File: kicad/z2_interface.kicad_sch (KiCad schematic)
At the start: 0 parts

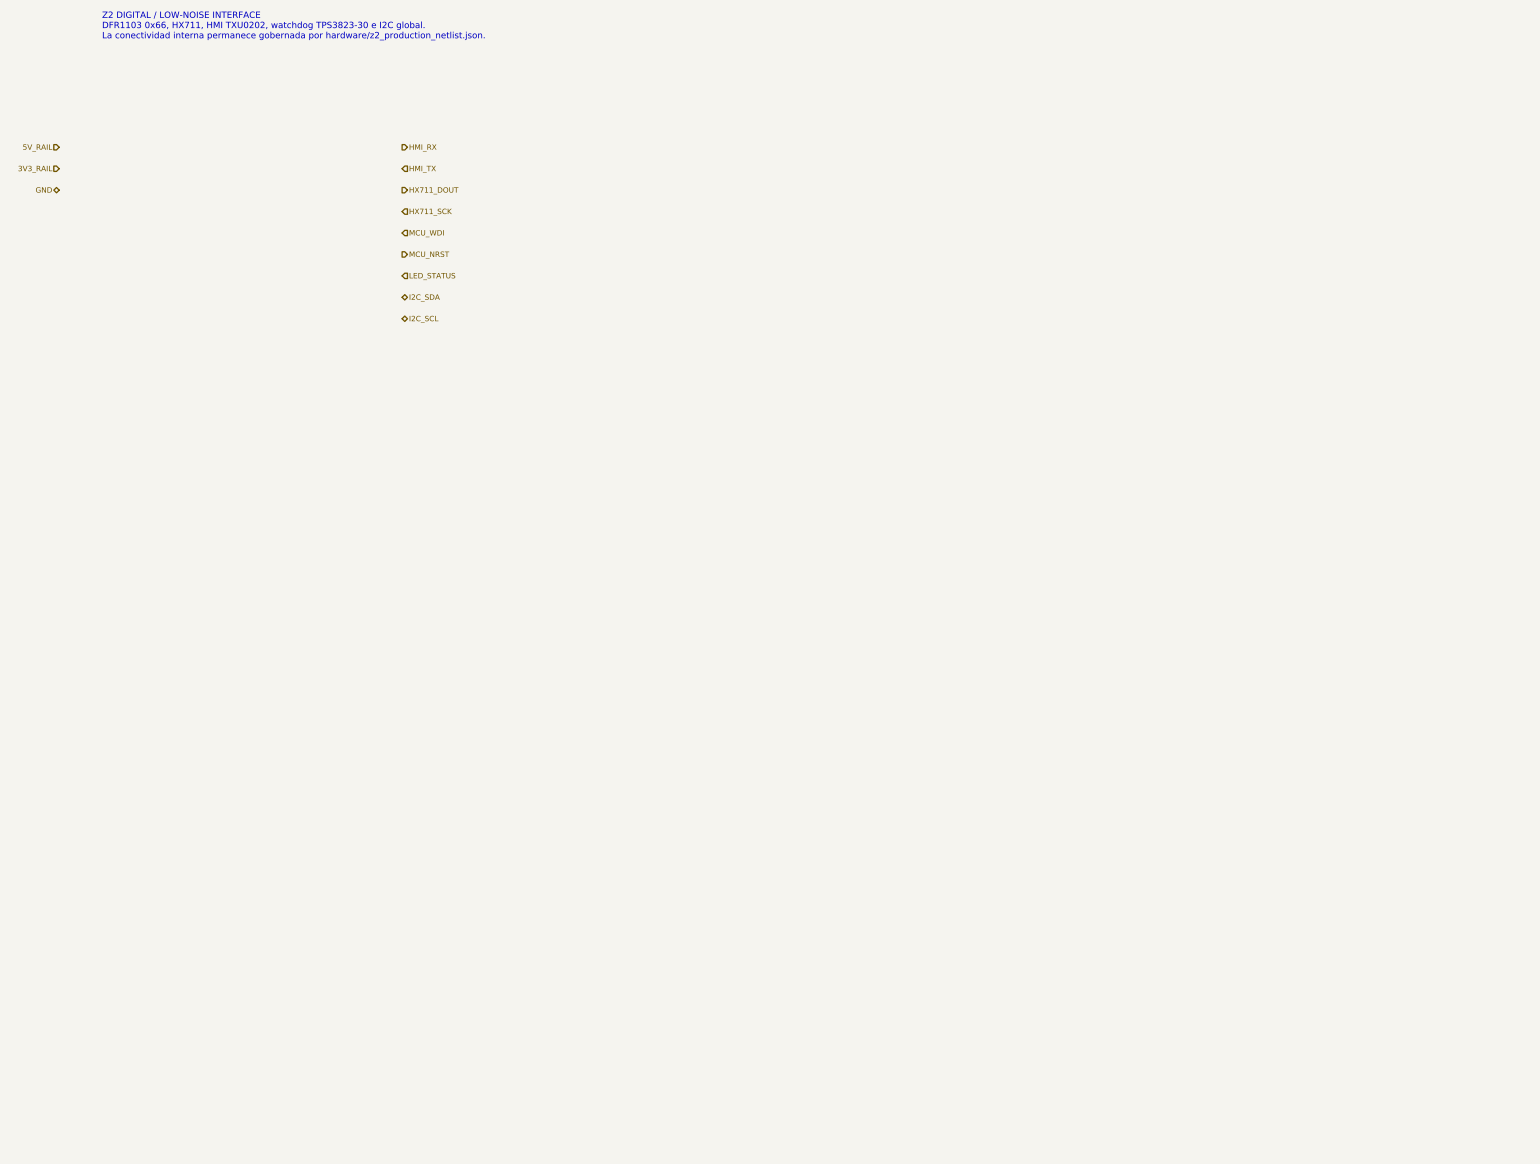
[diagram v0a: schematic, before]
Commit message: eda: materializar hierarchy de producción y cerrar ERC en cero (#15)
Materializa Z0–Z4 de forma determinista desde JSON/BOM, registra NFB_GEN, cierra seis links físicos verificados, elimina la deuda ERC de PR #14 y congela ERC=0/0 antes de placement. Mantiene placement, routing y geometría PCB fuera de alcance.
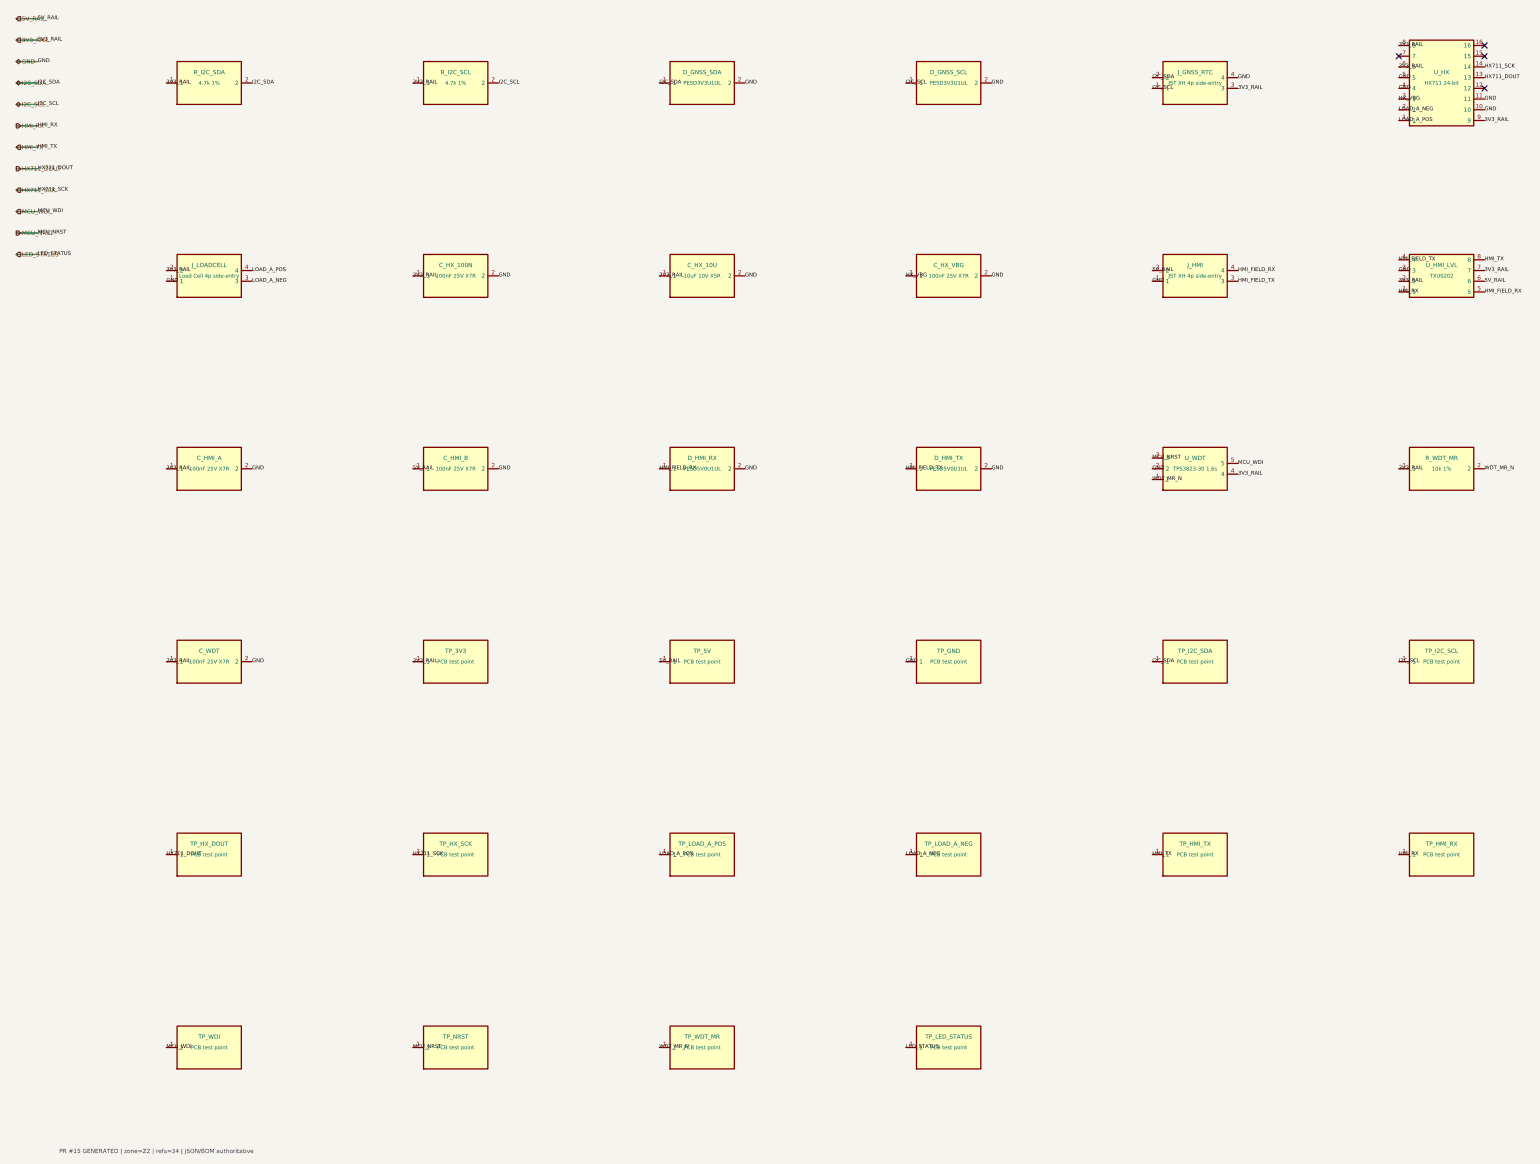
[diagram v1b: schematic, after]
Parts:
- added C_HMI_A: 100nF 25V X7R, Capacitor_SMD:C_0402_1005Metric, symbol NFB_GEN:SYM_C_HMI_A
- added C_HMI_B: 100nF 25V X7R, Capacitor_SMD:C_0402_1005Metric, symbol NFB_GEN:SYM_C_HMI_B
- added C_HX_100N: 100nF 25V X7R, Capacitor_SMD:C_0402_1005Metric, symbol NFB_GEN:SYM_C_HX_100N
- added C_HX_10U: 10uF 10V X5R, Capacitor_SMD:C_0805_2012Metric, symbol NFB_GEN:SYM_C_HX_10U
- added C_HX_VBG: 100nF 25V X7R, Capacitor_SMD:C_0402_1005Metric, symbol NFB_GEN:SYM_C_HX_VBG
- added C_WDT: 100nF 25V X7R, Capacitor_SMD:C_0402_1005Metric, symbol NFB_GEN:SYM_C_WDT
- added D_GNSS_SCL: PESD3V3U1UL, Diode_SMD:D_SOD-882, symbol NFB_GEN:SYM_D_GNSS_SCL
- added D_GNSS_SDA: PESD3V3U1UL, Diode_SMD:D_SOD-882, symbol NFB_GEN:SYM_D_GNSS_SDA
- added D_HMI_RX: PESD5V0U1UL, Diode_SMD:D_SOD-882, symbol NFB_GEN:SYM_D_HMI_RX
- added D_HMI_TX: PESD5V0U1UL, Diode_SMD:D_SOD-882, symbol NFB_GEN:SYM_D_HMI_TX
- added J_GNSS_RTC: JST XH 4p side-entry, Connector_JST:JST_XH_S4B-XH-A_1x04_P2.50mm_Horizontal, symbol NFB_GEN:SYM_J_GNSS_RTC
- added J_HMI: JST XH 4p side-entry, Connector_JST:JST_XH_S4B-XH-A_1x04_P2.50mm_Horizontal, symbol NFB_GEN:SYM_J_HMI
- added J_LOADCELL: Load Cell 4p side-entry, TerminalBlock_Phoenix:TerminalBlock_Phoenix_PT-1,5-4-5.0-H_1x04_P5.00mm_Horizontal, symbol NFB_GEN:SYM_J_LOADCELL
- added R_I2C_SCL: 4.7k 1%, Resistor_SMD:R_0402_1005Metric, symbol NFB_GEN:SYM_R_I2C_SCL
- added R_I2C_SDA: 4.7k 1%, Resistor_SMD:R_0402_1005Metric, symbol NFB_GEN:SYM_R_I2C_SDA
- added R_WDT_MR: 10k 1%, Resistor_SMD:R_0402_1005Metric, symbol NFB_GEN:SYM_R_WDT_MR
- added TP_3V3: PCB test point, TestPoint:TestPoint_Pad_D1.0mm, symbol NFB_GEN:SYM_TP_3V3
- added TP_5V: PCB test point, TestPoint:TestPoint_Pad_D1.0mm, symbol NFB_GEN:SYM_TP_5V
- added TP_GND: PCB test point, TestPoint:TestPoint_Pad_D1.0mm, symbol NFB_GEN:SYM_TP_GND
- added TP_HMI_RX: PCB test point, TestPoint:TestPoint_Pad_D1.0mm, symbol NFB_GEN:SYM_TP_HMI_RX
- added TP_HMI_TX: PCB test point, TestPoint:TestPoint_Pad_D1.0mm, symbol NFB_GEN:SYM_TP_HMI_TX
- added TP_HX_DOUT: PCB test point, TestPoint:TestPoint_Pad_D1.0mm, symbol NFB_GEN:SYM_TP_HX_DOUT
- added TP_HX_SCK: PCB test point, TestPoint:TestPoint_Pad_D1.0mm, symbol NFB_GEN:SYM_TP_HX_SCK
- added TP_I2C_SCL: PCB test point, TestPoint:TestPoint_Pad_D1.0mm, symbol NFB_GEN:SYM_TP_I2C_SCL
- added TP_I2C_SDA: PCB test point, TestPoint:TestPoint_Pad_D1.0mm, symbol NFB_GEN:SYM_TP_I2C_SDA
- added TP_LED_STATUS: PCB test point, TestPoint:TestPoint_Pad_D1.0mm, symbol NFB_GEN:SYM_TP_LED_STATUS
- added TP_LOAD_A_NEG: PCB test point, TestPoint:TestPoint_Pad_D1.0mm, symbol NFB_GEN:SYM_TP_LOAD_A_NEG
- added TP_LOAD_A_POS: PCB test point, TestPoint:TestPoint_Pad_D1.0mm, symbol NFB_GEN:SYM_TP_LOAD_A_POS
- added TP_NRST: PCB test point, TestPoint:TestPoint_Pad_D1.0mm, symbol NFB_GEN:SYM_TP_NRST
- added TP_WDI: PCB test point, TestPoint:TestPoint_Pad_D1.0mm, symbol NFB_GEN:SYM_TP_WDI
- added TP_WDT_MR: PCB test point, TestPoint:TestPoint_Pad_D1.0mm, symbol NFB_GEN:SYM_TP_WDT_MR
- added U_HMI_LVL: TXU0202, NFB:TI_DCU0008A_TXU0202, symbol NFB_GEN:SYM_U_HMI_LVL
- added U_HX: HX711 24-bit, Package_SO:SOP-16_4.4x10.4mm_P1.27mm, symbol NFB_GEN:SYM_U_HX
- added U_WDT: TPS3823-30 1.6s, Package_TO_SOT_SMD:SOT-23-5, symbol NFB_GEN:SYM_U_WDT
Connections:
- net 3V3_RAIL: now also C_HMI_A.1, C_HX_100N.1, C_HX_10U.1, C_WDT.1, J_GNSS_RTC.3, J_LOADCELL.2, R_I2C_SCL.1, R_I2C_SDA.1, R_WDT_MR.1, TP_3V3.1, U_HMI_LVL.2, U_HMI_LVL.7, U_HX.6, U_HX.8, U_HX.9, U_WDT.4
- net 5V_RAIL: now also C_HMI_B.1, J_HMI.2, TP_5V.1, U_HMI_LVL.6
- net GND: now also C_HMI_A.2, C_HMI_B.2, C_HX_100N.2, C_HX_10U.2, C_HX_VBG.2, C_WDT.2, D_GNSS_SCL.2, D_GNSS_SDA.2, D_HMI_RX.2, D_HMI_TX.2, J_GNSS_RTC.4, J_HMI.1, J_LOADCELL.1, TP_GND.1, U_HMI_LVL.3, U_HX.10, U_HX.11, U_HX.4, U_HX.5, U_WDT.2
- net HMI_RX: now also TP_HMI_RX.1, U_HMI_LVL.1
- net HMI_TX: now also TP_HMI_TX.1, U_HMI_LVL.8
- net HX711_DOUT: now also TP_HX_DOUT.1, U_HX.13
- net HX711_SCK: now also TP_HX_SCK.1, U_HX.14
- net I2C_SCL: now also D_GNSS_SCL.1, J_GNSS_RTC.1, R_I2C_SCL.2, TP_I2C_SCL.1
- net I2C_SDA: now also D_GNSS_SDA.1, J_GNSS_RTC.2, R_I2C_SDA.2, TP_I2C_SDA.1
- net LED_STATUS: now also TP_LED_STATUS.1
- net MCU_NRST: now also TP_NRST.1, U_WDT.3
- net MCU_WDI: now also TP_WDI.1, U_WDT.5
- new net HMI_FIELD_RX: D_HMI_RX.1, J_HMI.4, U_HMI_LVL.5
- new net HMI_FIELD_TX: D_HMI_TX.1, J_HMI.3, U_HMI_LVL.4
- new net HX_VBG: C_HX_VBG.1, U_HX.3
- new net LOAD_A_NEG: J_LOADCELL.3, TP_LOAD_A_NEG.1, U_HX.2
- new net LOAD_A_POS: J_LOADCELL.4, TP_LOAD_A_POS.1, U_HX.1
- new net WDT_MR_N: R_WDT_MR.2, TP_WDT_MR.1, U_WDT.1
- no-connect marks 0 -> 4
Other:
- note added: "PR #15 GENERATED | zone=Z2 | refs=34 | JSON/BOM authoritative"
- note removed: "Z2 DIGITAL / LOW-NOISE INTERFACE DFR1103 0x66, HX711, HMI TXU0202, watchdog TPS3823-30 e I2C global. La conectividad interna permanece gobernada por hardware/z2_production_netlist.json."
- title: NFB Insight PCBA v2 — Z2 Interface -> NFB Insight PCBA v2 — Z2 GENERATED PRODUCTION

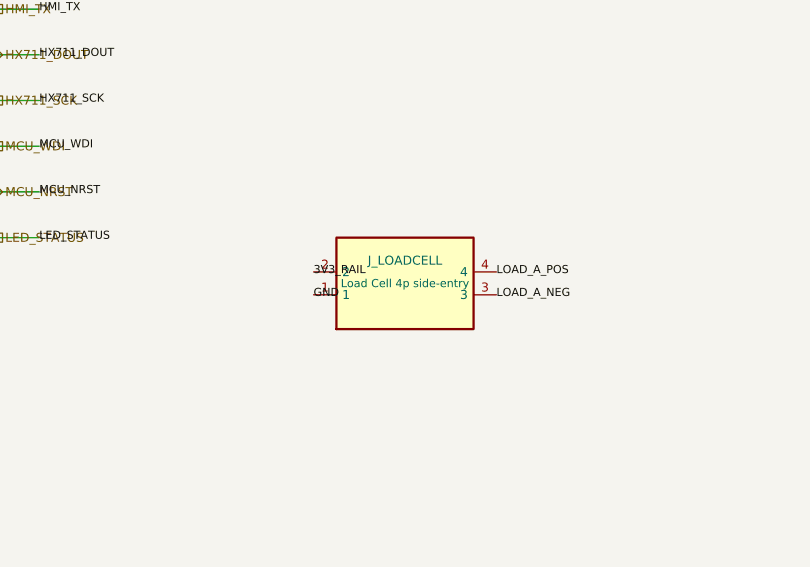
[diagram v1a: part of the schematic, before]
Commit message: bom: materializar Phoenix 1757268 en Z2 PR16
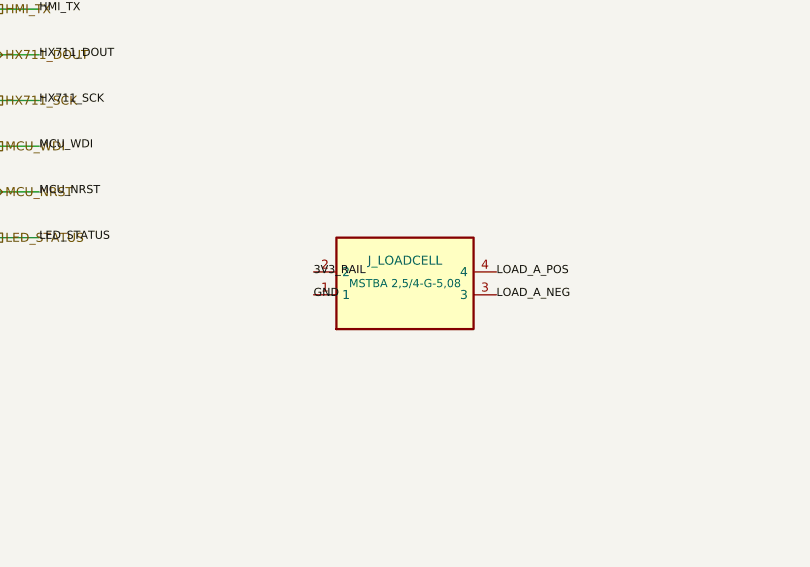
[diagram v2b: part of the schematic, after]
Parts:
- J_LOADCELL: value Load Cell 4p side-entry -> MSTBA 2,5/4-G-5,08; footprint TerminalBlock_Phoenix:TerminalBlock_Phoenix_PT-1,5-4-5.0-H_1x04_P5.00mm_Horizontal -> Connector_Phoenix_MSTB:PhoenixContact_MSTBA_2,5_4-G-5,08_1x04_P5.08mm_Horizontal; MPN Phoenix PT-1,5-4-5.0-H -> 1757268
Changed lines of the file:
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@@
     (exclude_from_sim yes) (in_bom yes) (on_board yes) (dnp no)
     (property "Reference" "J_LOADCELL" (at 55.88 78.74 0) (effects (font (size 1 1))))
-    (property "Value" "Load Cell 4p side-entry" (at 55.88 81.28 0) (effects (font (size 0.9 0.9))))
-    (property "Footprint" "TerminalBlock_Phoenix:TerminalBlock_Phoenix_PT-1,5-4-5.0-H_1x04_P5.00mm_Horizontal" (at 55.88 83.82 0) (effects (font (size 0.8 0.8)) (hide yes)))
+    (property "Value" "MSTBA 2,5/4-G-5,08" (at 55.88 81.28 0) (effects (font (size 0.9 0.9))))
+    (property "Footprint" "Connector_Phoenix_MSTB:PhoenixContact_MSTBA_2,5_4-G-5,08_1x04_P5.08mm_Horizontal" (at 55.88 83.82 0) (effects (font (size 0.8 0.8)) (hide yes)))
     (property "Datasheet" "~" (at 55.88 81.28 0) (effects (font (size 0.8 0.8)) (hide yes)))
-    (property "MPN" "Phoenix PT-1,5-4-5.0-H" (at 55.88 86.36 0) (effects (font (size 0.8 0.8)) (hide yes)))
+    (property "MPN" "1757268" (at 55.88 86.36 0) (effects (font (size 0.8 0.8)) (hide yes)))
     (pin "1")
     (pin "2")

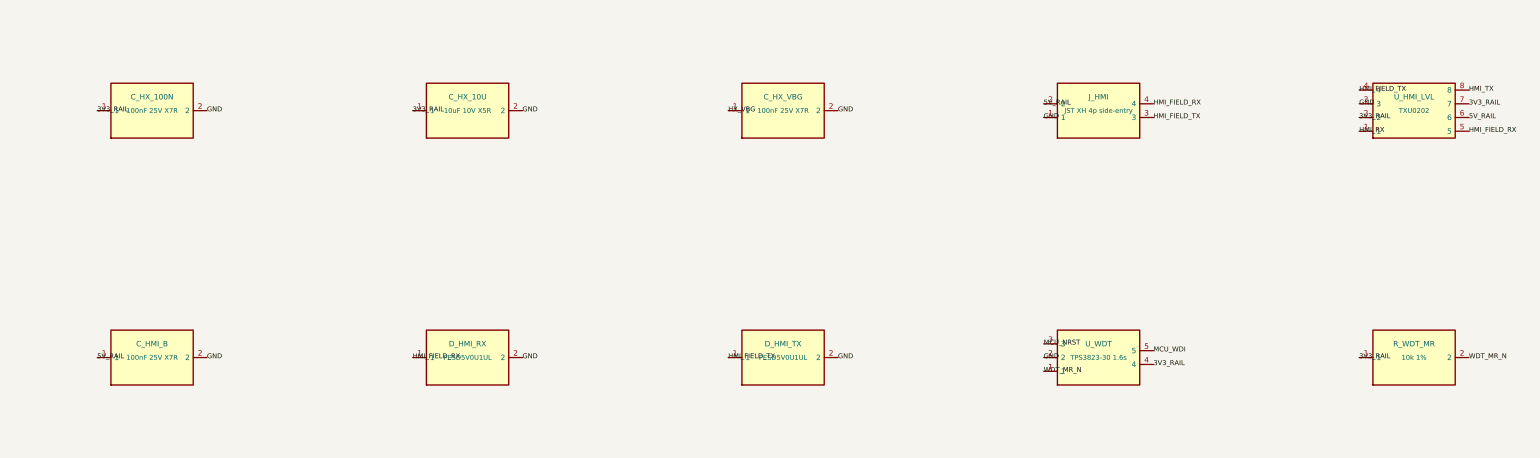
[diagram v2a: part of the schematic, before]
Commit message: power: cerrar ECO HMI con 5V_HMI dedicado y PR19D
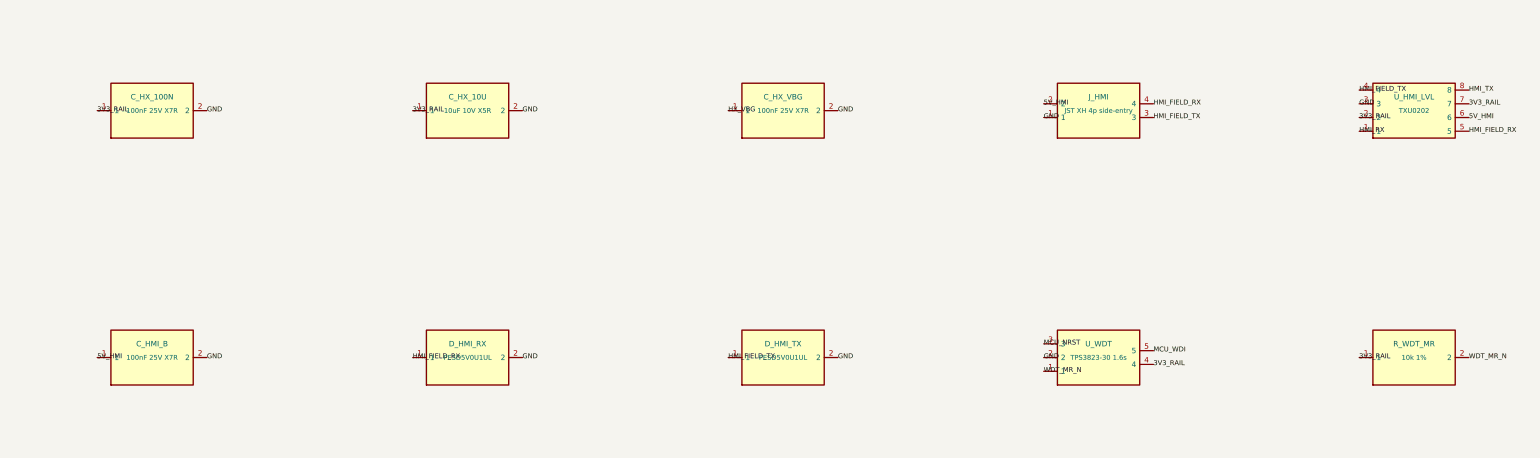
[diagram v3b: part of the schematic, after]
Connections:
- net 5V_RAIL: no longer C_HMI_B.1, J_HMI.2, U_HMI_LVL.6
- new net 5V_HMI: C_HMI_B.1, J_HMI.2, U_HMI_LVL.6
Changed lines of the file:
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@@
     (instances (project "NFB_Insight_PCBA_v2" (path "/8d1b8c9c-4f38-4be9-a83e-5bd34c8eef41/bb6d2e1e-0e72-4b22-a186-53eb5a676b33" (reference "J_HMI") (unit 1))))
   )
-  (label "5V_RAIL" (at 279.4 80.01 0)
+  (label "5V_HMI" (at 279.4 80.01 0)
     (effects (font (size 0.9 0.9)) (justify left))
 )
@@
     (effects (font (size 0.9 0.9)) (justify left))
 )
-  (label "5V_RAIL" (at 358.14 82.55 0)
+  (label "5V_HMI" (at 358.14 82.55 0)
     (effects (font (size 0.9 0.9)) (justify left))
 )
@@
     (instances (project "NFB_Insight_PCBA_v2" (path "/8d1b8c9c-4f38-4be9-a83e-5bd34c8eef41/bb6d2e1e-0e72-4b22-a186-53eb5a676b33" (reference "C_HMI_B") (unit 1))))
   )
-  (label "5V_RAIL" (at 104.14 127 0)
+  (label "5V_HMI" (at 104.14 127 0)
     (effects (font (size 0.9 0.9)) (justify left))
 )
